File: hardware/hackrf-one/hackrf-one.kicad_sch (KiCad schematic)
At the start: 0 parts

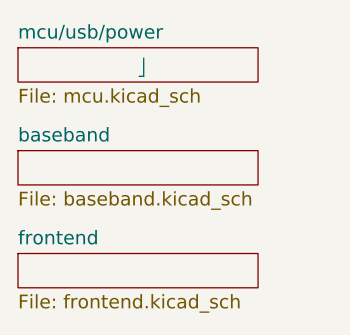
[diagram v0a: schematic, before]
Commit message: Attempts to resolve wierd legacy ERC errors
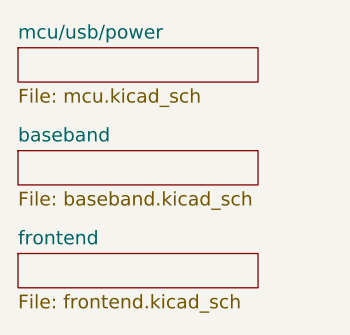
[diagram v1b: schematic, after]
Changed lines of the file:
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@@
 		(comment 1 "License: GPL v2")
-	)
-	(wire
-		(pts
-			(xy 78.232 64.135) (xy 78.74 64.135)
-		)
-		(stroke
-			(width 0)
-			(type default)
-		)
-	)
-	(wire
-		(pts
-			(xy 78.74 64.135) (xy 78.74 62.103)
-		)
-		(stroke
-			(width 0)
-			(type default)
-		)
 	)
 	(sheet
